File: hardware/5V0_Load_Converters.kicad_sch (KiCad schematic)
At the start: 78 parts, among them J19 61300311121, Q26 EPC2016C, Q27 EPC2016C, Q8 SI2302DDS-T1-GE3, U21 INA199C3DCKR, U30 LTC3833EUDC-TRPBF

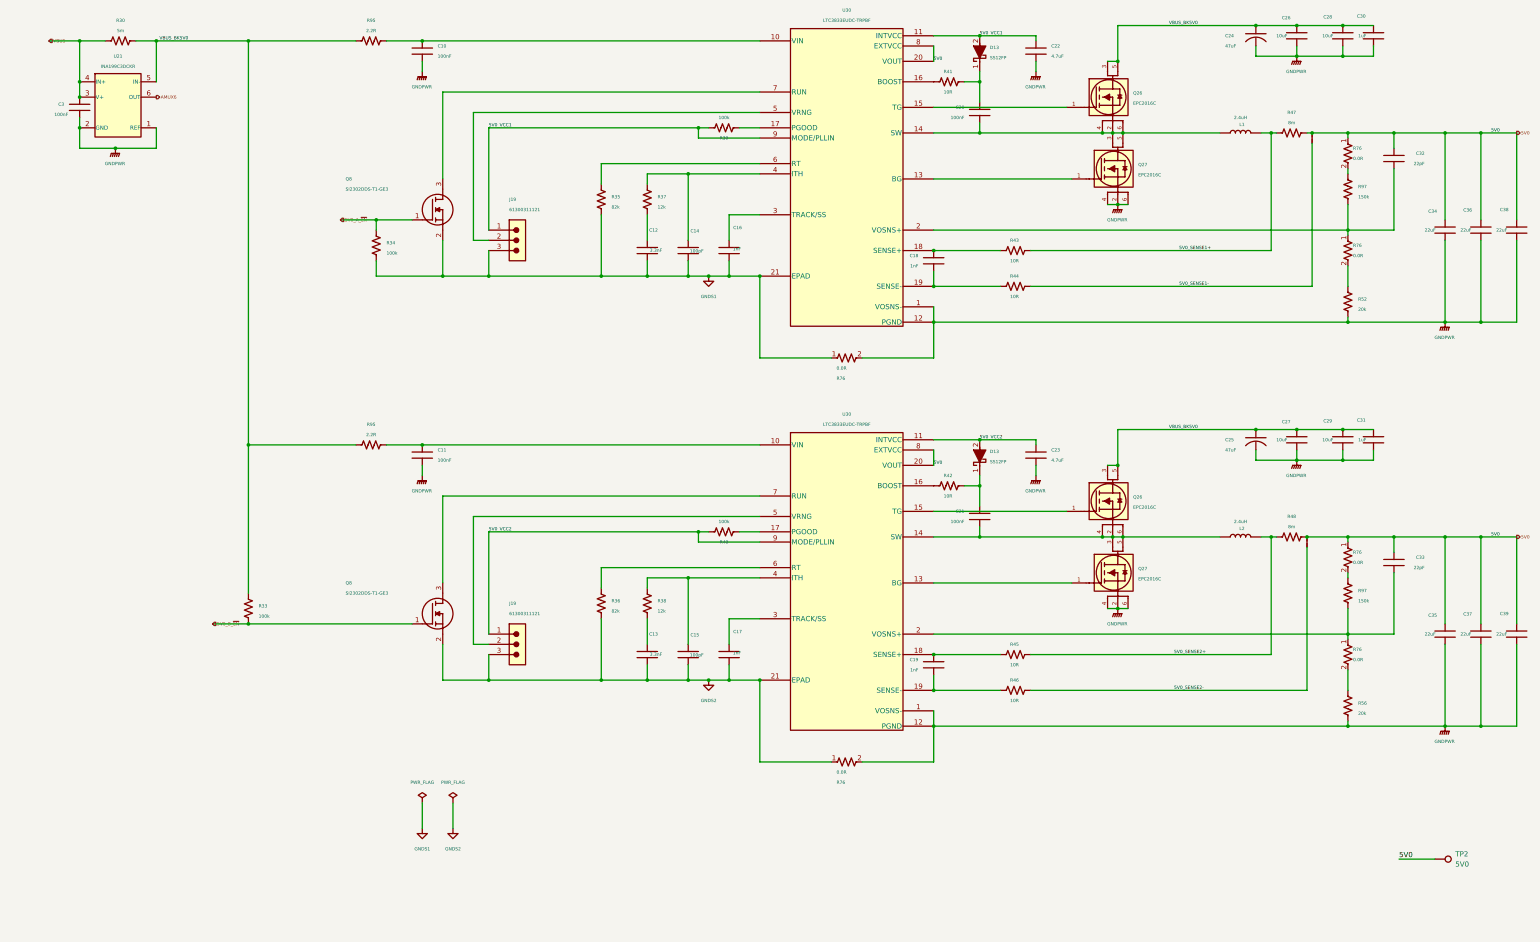
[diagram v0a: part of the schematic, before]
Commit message: hardware: Improving the readability of schematics
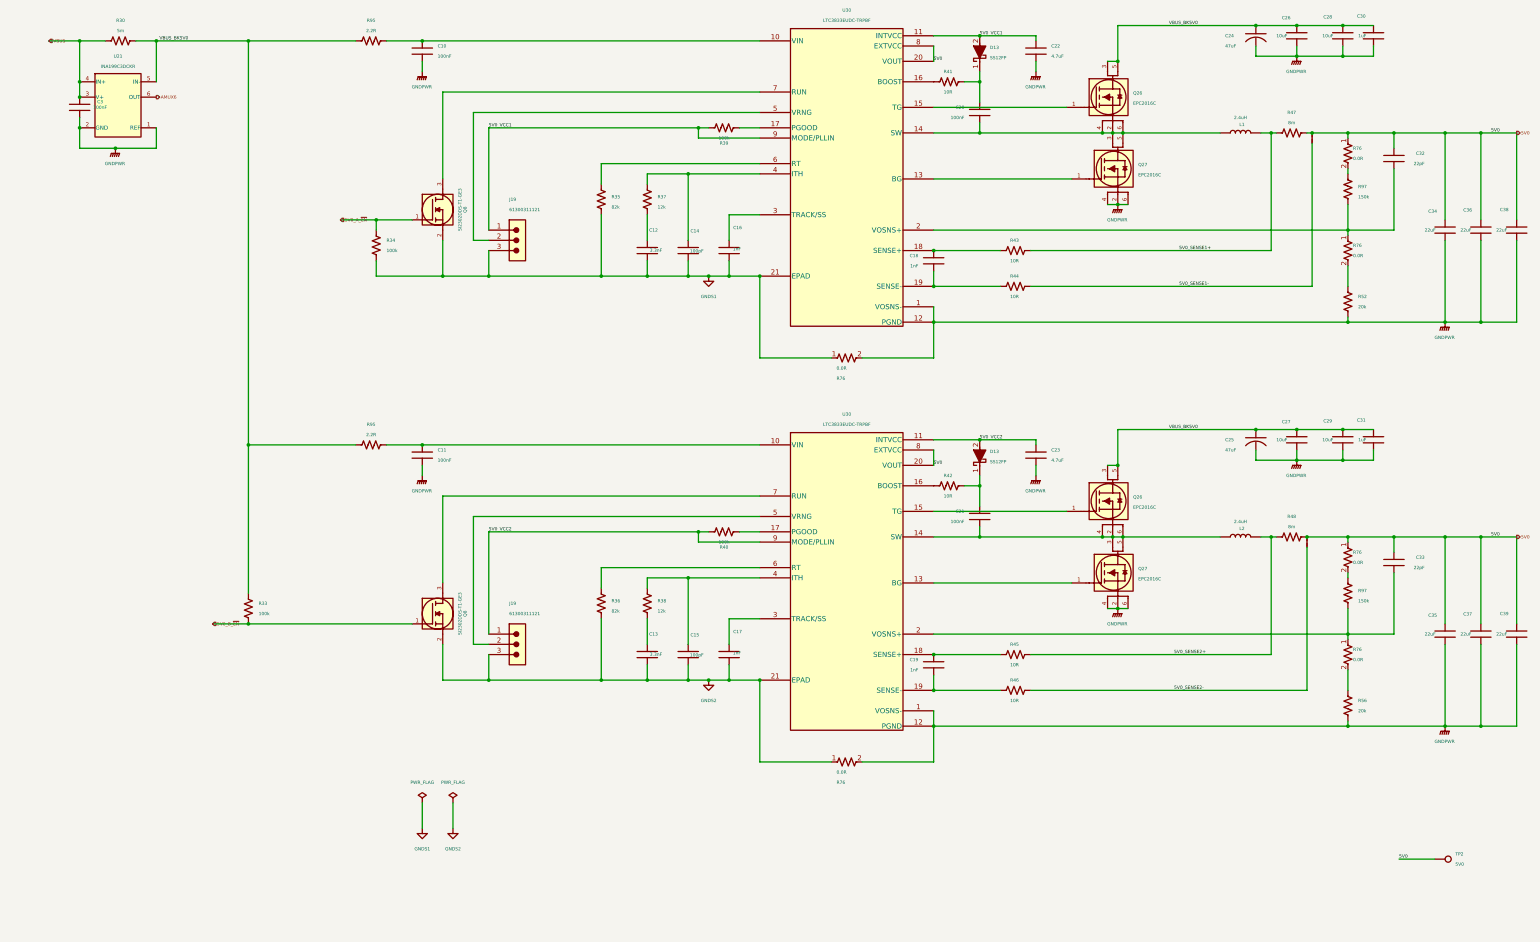
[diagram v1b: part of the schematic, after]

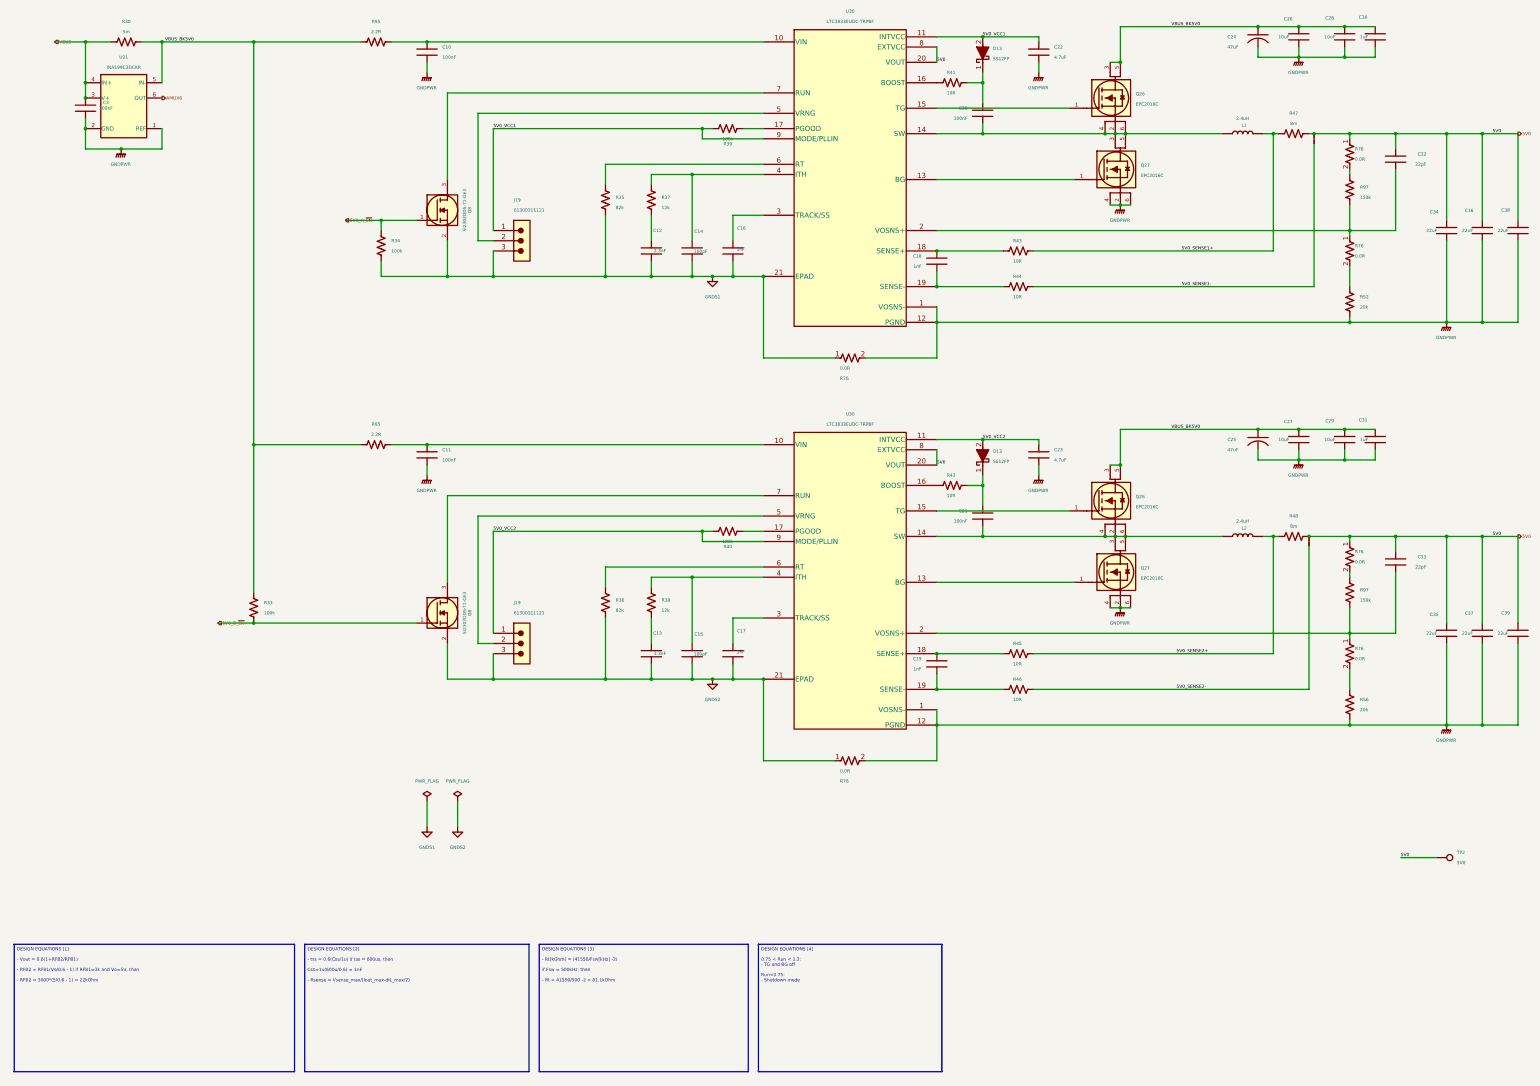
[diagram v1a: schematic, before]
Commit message: hardware: Increasing the readability of the schematic and adding a table with the revision history
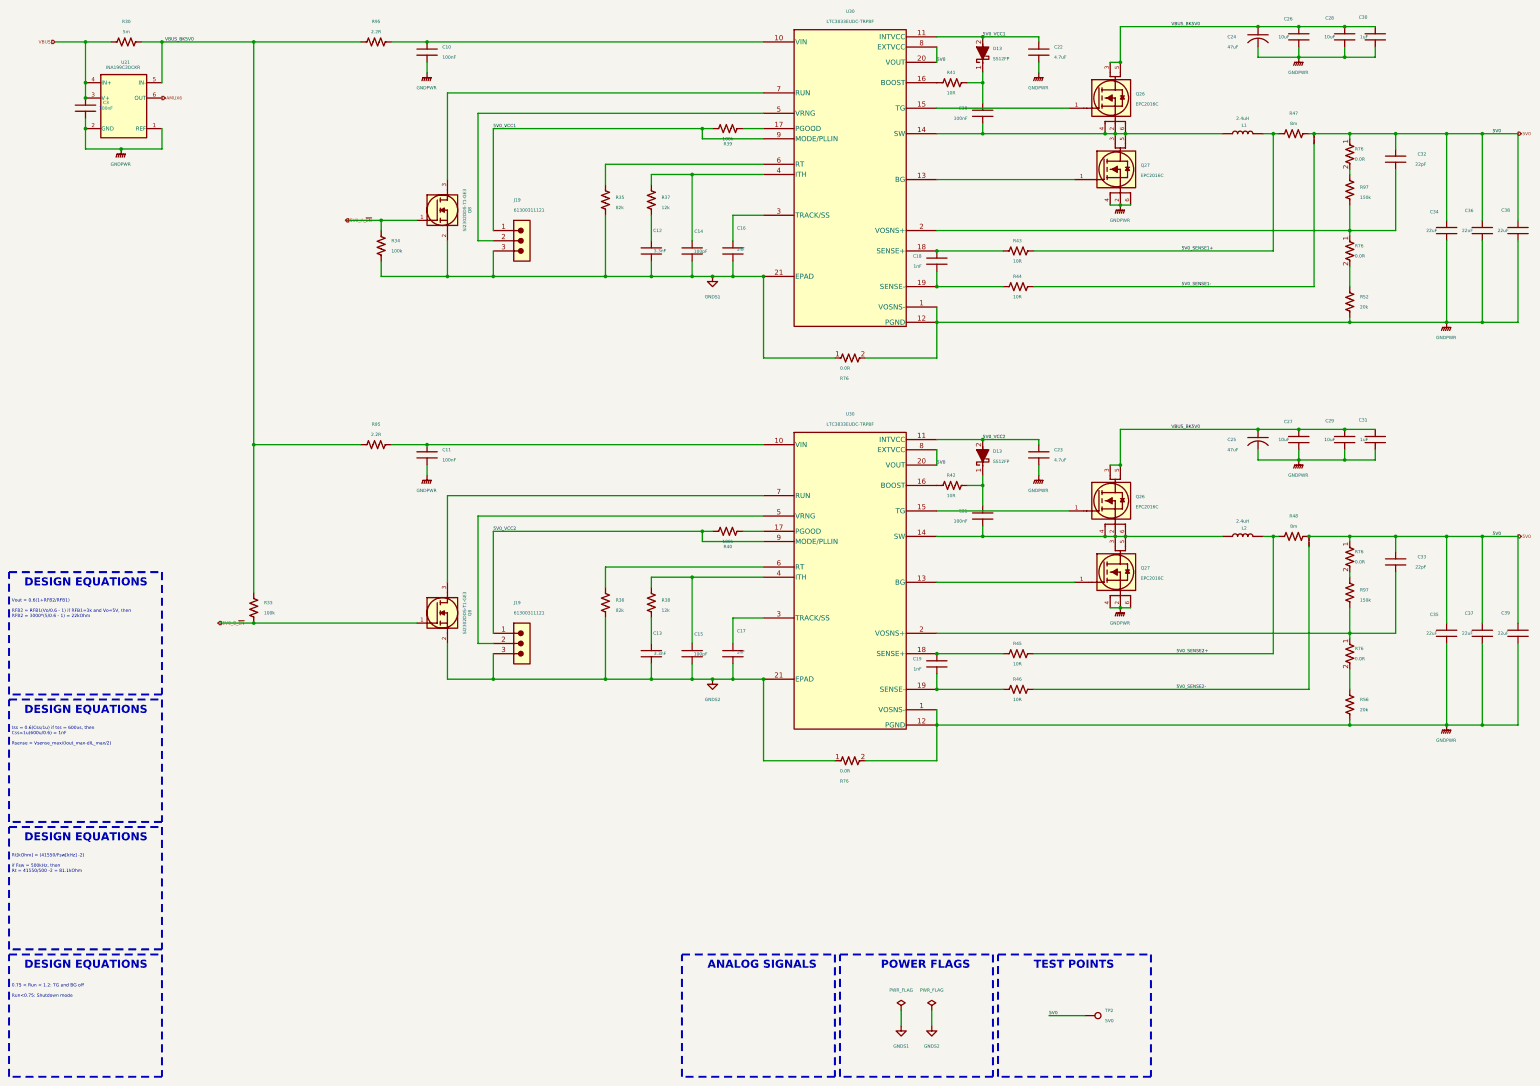
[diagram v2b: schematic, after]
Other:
- note added: "ANALOG SIGNALS"
- note added: "DESIGN EQUATIONS"
- note added: "POWER FLAGS"
- note added: "TEST POINTS"
- moved on the sheet: TP2

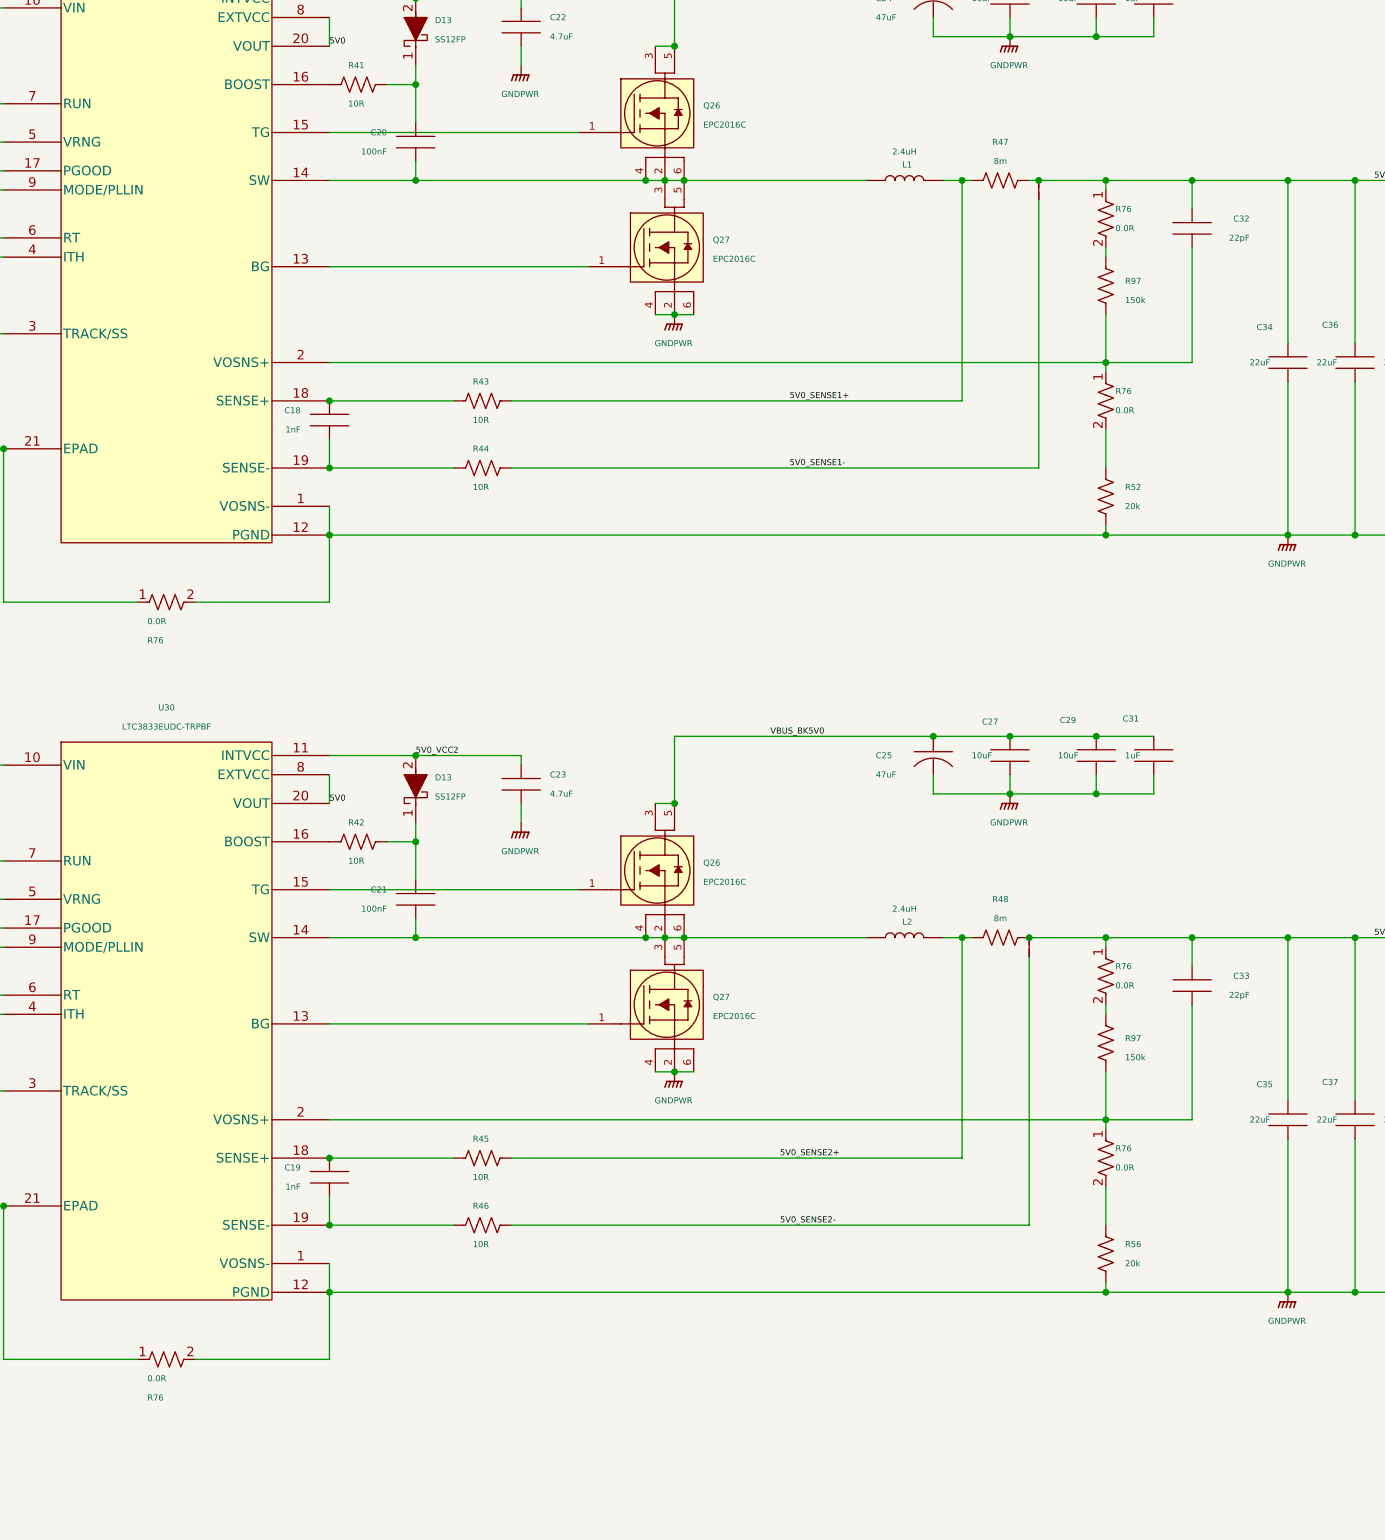
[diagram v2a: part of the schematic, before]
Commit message: hardware: Improving the readability of schematic
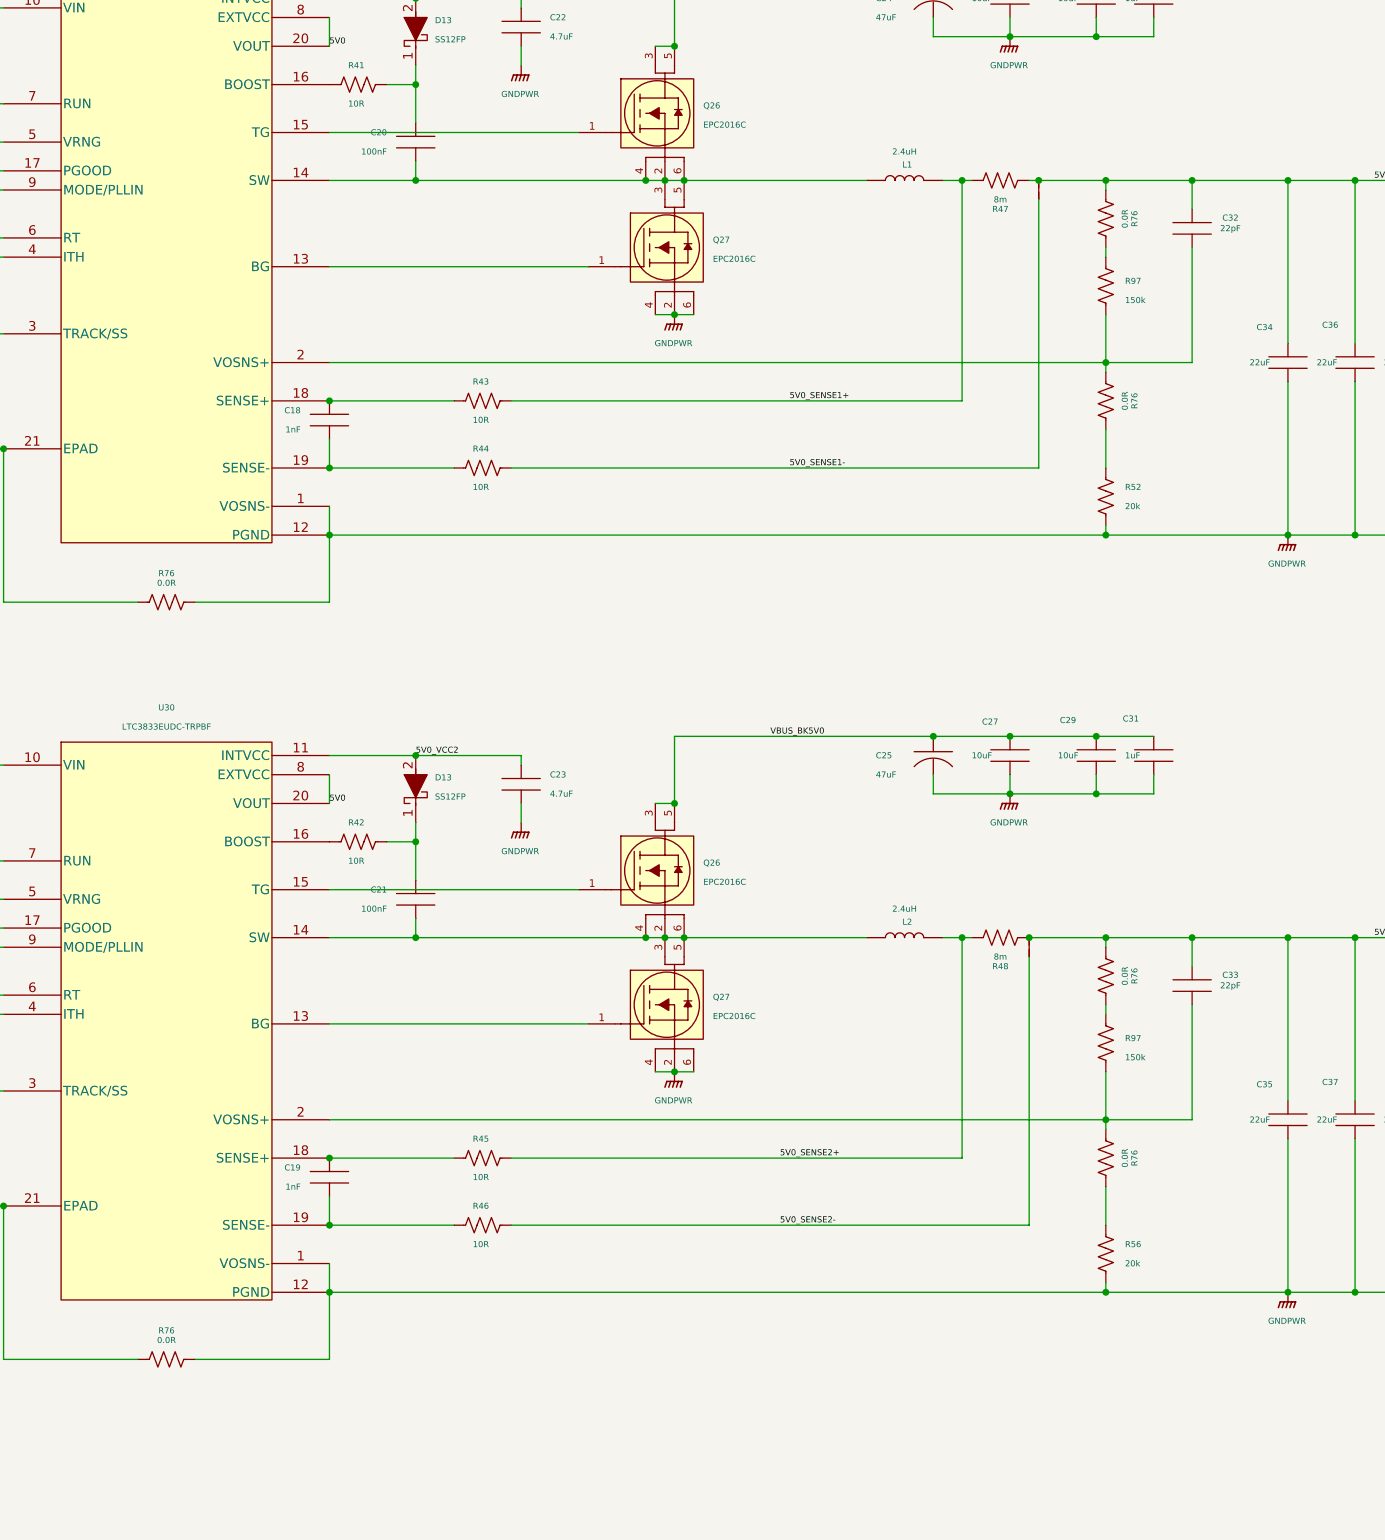
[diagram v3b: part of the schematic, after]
